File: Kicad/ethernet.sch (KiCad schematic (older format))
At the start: 26 parts, among them J12 RJ45_Amphenol_RJMG1BD3B8K1ANR, U11 DP83848C

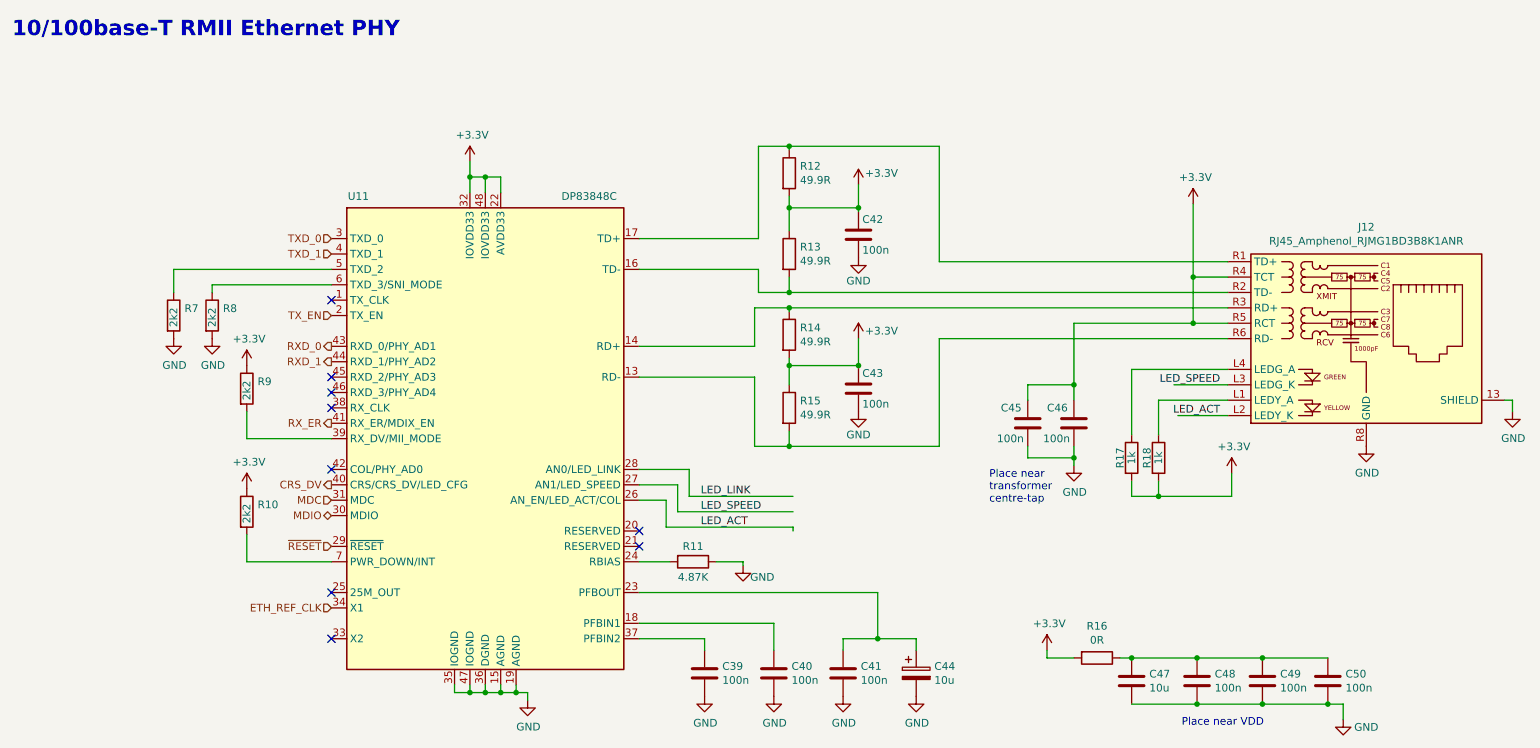
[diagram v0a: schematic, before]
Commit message: Removed USB FS hub. Added stacked USB A connector.
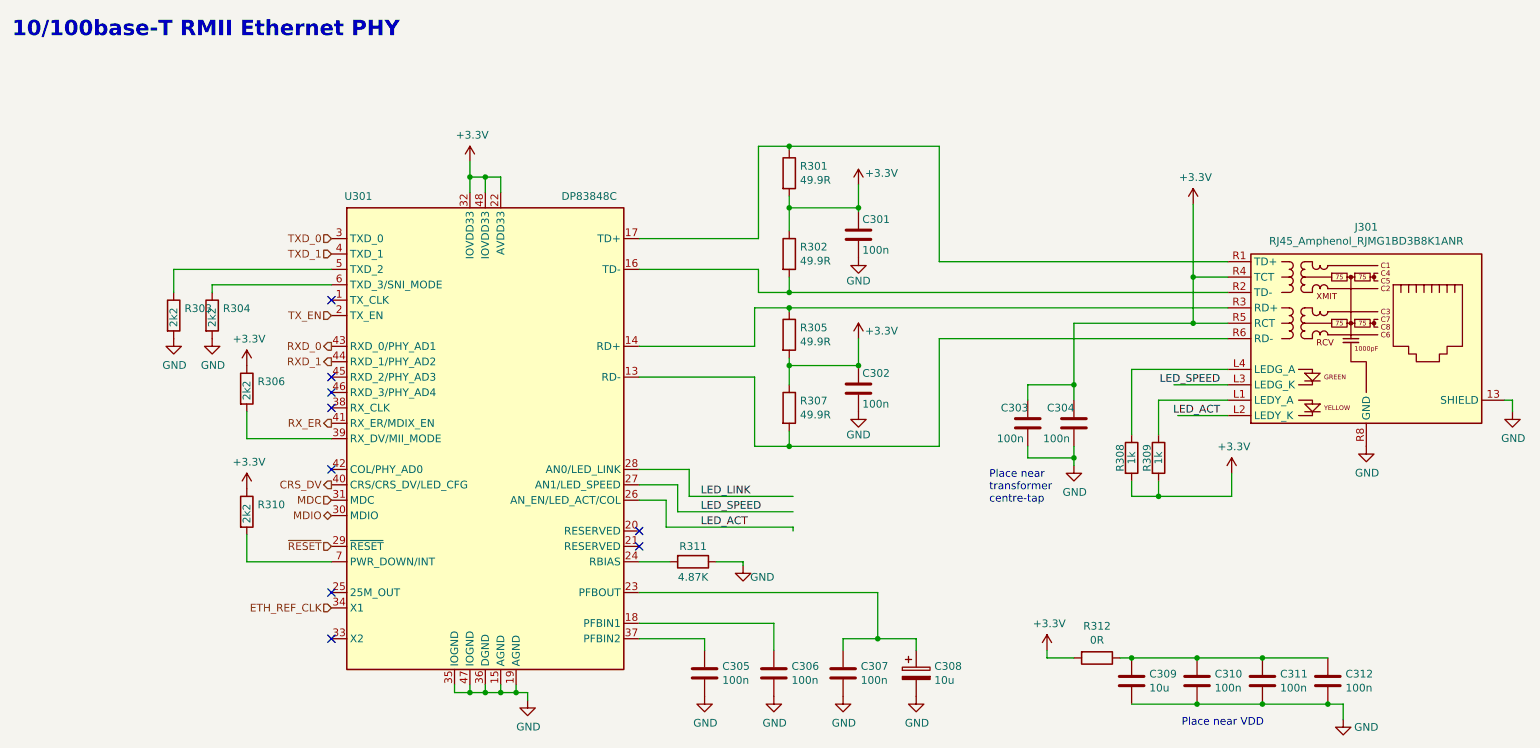
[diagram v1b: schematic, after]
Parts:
- C309: renamed from C47; footprint Capacitor_SMD:C_0402_1005Metric -> Capacitor_SMD:C_0805_2012Metric
- R301: renamed from R12; footprint (none) -> Resistor_SMD:R_0402_1005Metric
- R302: renamed from R13; footprint (none) -> Resistor_SMD:R_0402_1005Metric
- R303: renamed from R7; footprint (none) -> Resistor_SMD:R_0402_1005Metric
- R304: renamed from R8; footprint (none) -> Resistor_SMD:R_0402_1005Metric
- R305: renamed from R14; footprint (none) -> Resistor_SMD:R_0402_1005Metric
- R306: renamed from R9; footprint (none) -> Resistor_SMD:R_0402_1005Metric
- R307: renamed from R15; footprint (none) -> Resistor_SMD:R_0402_1005Metric
- R308: renamed from R17; footprint (none) -> Resistor_SMD:R_0402_1005Metric
- R309: renamed from R18; footprint (none) -> Resistor_SMD:R_0402_1005Metric
- R310: renamed from R10; footprint (none) -> Resistor_SMD:R_0402_1005Metric
- R311: renamed from R11; footprint (none) -> Resistor_SMD:R_0402_1005Metric
- R312: renamed from R16; footprint (none) -> Resistor_SMD:R_0402_1005Metric
- renumbered C42 to C301, C43 to C302, C45 to C303, C46 to C304, C39 to C305, C40 to C306, C41 to C307, C44 to C308, C48 to C310, C49 to C311, C50 to C312, J12 to J301, U11 to U301

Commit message: Schematic updates
Worked on USB Hub
Deleted QSPI SRAM
Added TSSOP-54 SDRAM (not wired up)
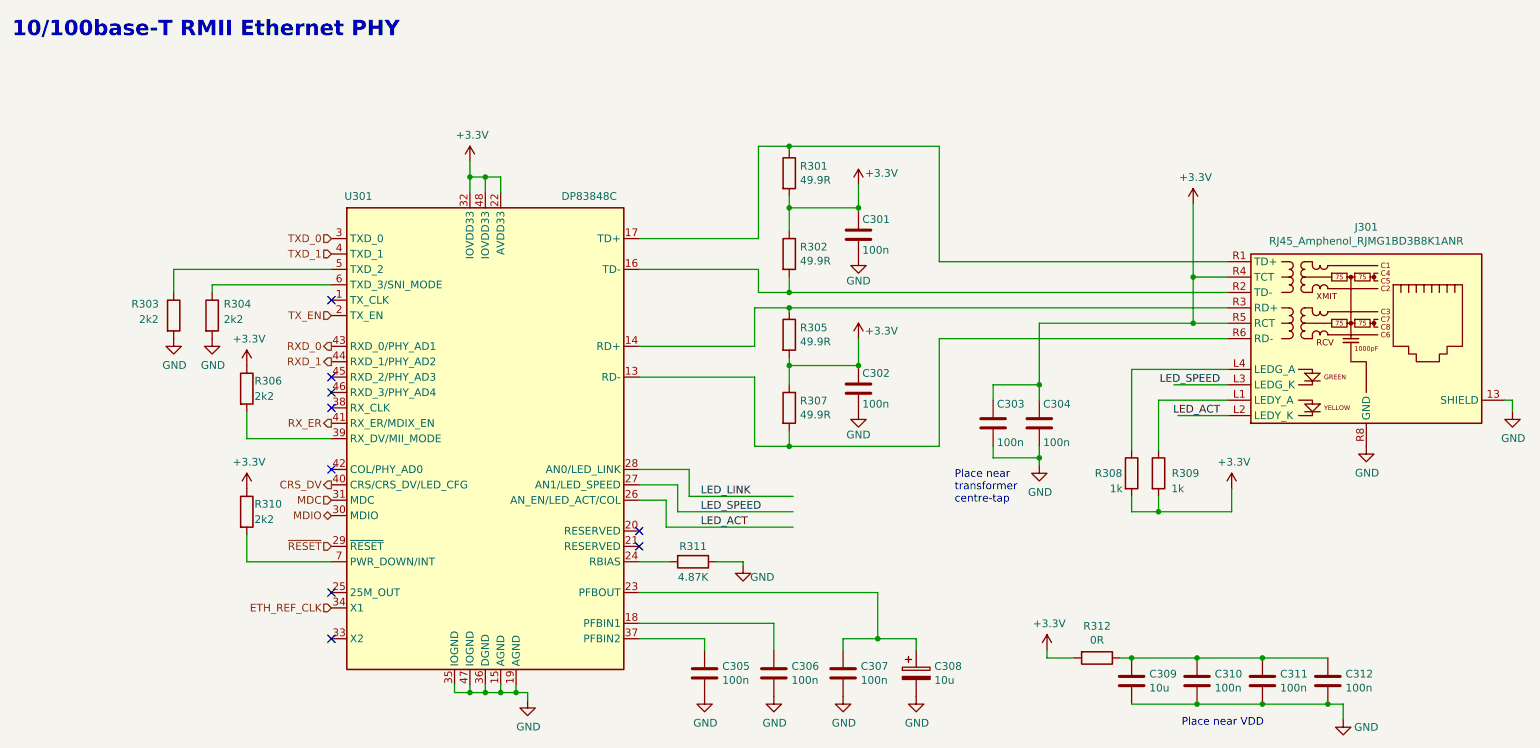
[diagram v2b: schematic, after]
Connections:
- wire segments 118 -> 117
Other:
- moved on the sheet: C303, C304, R308, R309
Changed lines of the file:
@@
 $Descr A4 11693 8268
 encoding utf-8
-Sheet 2 6
+Sheet 2 5
 Title "Neotron F7"
 Date "2020-05-25"
@@
 L Device:C C304
 U 1 1 5FA9EAF1
-P 7475 3275
-F 0 "C304" H 7300 3375 50  0000 L CNN
-F 1 "100n" H 7275 3175 50  0000 L CNN
-F 2 "Capacitor_SMD:C_0402_1005Metric" H 7513 3125 50  0001 C CNN
-F 3 "~" H 7475 3275 50  0001 C CNN
-F 4 "C1546" H 7475 3275 50  0001 C CNN "LCSC"
-	1    7475 3275
+P 7250 3275
+F 0 "C304" H 7275 3400 50  0000 L CNN
+F 1 "100n" H 7275 3150 50  0000 L CNN
+F 2 "Capacitor_SMD:C_0402_1005Metric" H 7288 3125 50  0001 C CNN
+F 3 "~" H 7250 3275 50  0001 C CNN
+F 4 "C1546" H 7250 3275 50  0001 C CNN "LCSC"
+	1    7250 3275
 	1    0    0    -1
 $EndComp
@@
 L Device:C C303
 U 1 1 5FA9EEAC
-P 7175 3275
-F 0 "C303" H 7000 3375 50  0000 L CNN
-F 1 "100n" H 6975 3175 50  0000 L CNN
-F 2 "Capacitor_SMD:C_0402_1005Metric" H 7213 3125 50  0001 C CNN
-F 3 "~" H 7175 3275 50  0001 C CNN
-F 4 "C1546" H 7175 3275 50  0001 C CNN "LCSC"
-	1    7175 3275
+P 6950 3275
+F 0 "C303" H 6975 3400 50  0000 L CNN
+F 1 "100n" H 6975 3150 50  0000 L CNN
+F 2 "Capacitor_SMD:C_0402_1005Metric" H 6988 3125 50  0001 C CNN
+F 3 "~" H 6950 3275 50  0001 C CNN
+F 4 "C1546" H 6950 3275 50  0001 C CNN "LCSC"
+	1    6950 3275
 	1    0    0    -1
 $EndComp
@@
 L power:GND #PWR0312
 U 1 1 5FA9F4E3
-P 7475 3550
-F 0 "#PWR0312" H 7475 3300 50  0001 C CNN
-F 1 "GND" H 7480 3377 50  0000 C CNN
-F 2 "" H 7475 3550 50  0001 C CNN
-F 3 "" H 7475 3550 50  0001 C CNN
-	1    7475 3550
+P 7250 3550
+F 0 "#PWR0312" H 7250 3300 50  0001 C CNN
+F 1 "GND" H 7255 3377 50  0000 C CNN
+F 2 "" H 7250 3550 50  0001 C CNN
+F 3 "" H 7250 3550 50  0001 C CNN
+	1    7250 3550
 	1    0    0    -1
 $EndComp
@@
 Connection ~ 5625 2900
 Connection ~ 6075 2900
-$Comp
-L power:+3.3V #PWR0313
-U 1 1 5FB0F0ED
-P 8500 3600
-F 0 "#PWR0313" H 8500 3450 50  0001 C CNN
-F 1 "+3.3V" H 8515 3773 50  0000 C CNN
-F 2 "" H 8500 3600 50  0001 C CNN
-F 3 "" H 8500 3600 50  0001 C CNN
-	1    8500 3600
-	1    0    0    -1
-$EndComp
-$Comp
-L Device:R R309
-U 1 1 5FB10B30
-P 8025 3500
-F 0 "R309" V 7950 3500 50  0000 C CNN
-F 1 "1k" V 8025 3500 50  0000 C CNN
-F 2 "Resistor_SMD:R_0402_1005Metric" V 7955 3500 50  0001 C CNN
-F 3 "~" H 8025 3500 50  0001 C CNN
-	1    8025 3500
-	1    0    0    -1
-$EndComp
-$Comp
-L Device:R R308
-U 1 1 5FB11481
-P 7850 3500
-F 0 "R308" V 7775 3500 50  0000 C CNN
-F 1 "1k" V 7850 3500 50  0000 C CNN
-F 2 "Resistor_SMD:R_0402_1005Metric" V 7780 3500 50  0001 C CNN
-F 3 "~" H 7850 3500 50  0001 C CNN
-	1    7850 3500
-	1    0    0    -1
-$EndComp
 Text Label 8425 3025 2    50   ~ 0
 LED_SPEED
@@
 Wire Wire Line
 	4825 3950 5650 3950
-Wire Wire Line
-	5650 3950 5650 3975
 Text Label 5050 3750 0    50   ~ 0
 LED_LINK
@@
 Text Label 5050 3950 0    50   ~ 0
 LED_ACT
-Text Notes 6925 3800 0    50   ~ 0
+Text Notes 6700 3800 0    50   ~ 0
 Place near\ntransformer\ncentre-tap
 NoConn ~ 4650 3975
@@
 	8475 3225 8150 3225
 Wire Wire Line
-	7850 2925 7850 3350
-Wire Wire Line
-	7850 3750 7850 3650
-Wire Wire Line
-	8025 3650 8025 3750
-Wire Wire Line
 	8475 3025 8125 3025
-Wire Wire Line
-	7850 3750 8025 3750
 $Comp
 L power:GND #PWR0311
@@
 	10325 3125 10325 3200
 Wire Wire Line
-	8500 3750 8500 3600
-Wire Wire Line
 	7850 2925 8475 2925
-Connection ~ 8025 3750
-Wire Wire Line
-	8025 3750 8500 3750
 Wire Wire Line
 	8475 3125 8025 3125
 Wire Wire Line
-	8025 3125 8025 3350
-Wire Wire Line
-	7475 3025 7175 3025
-Connection ~ 7475 3025
+	7250 3025 6950 3025
+Connection ~ 7250 3025
 Wire Wire Line
 	8250 2325 8475 2325
-Wire Wire Line
-	7475 2625 8250 2625
 Wire Wire Line
 	8250 2325 8250 2625
@@
 U 1 1 5EDDE40E
 P 1875 2575
-F 0 "R304" H 1945 2621 50  0000 L CNN
-F 1 "2k2" V 1875 2500 50  0000 L CNN
+F 0 "R304" H 1950 2650 50  0000 L CNN
+F 1 "2k2" H 1950 2550 50  0000 L CNN
 F 2 "Resistor_SMD:R_0402_1005Metric" V 1805 2575 50  0001 C CNN
 F 3 "~" H 1875 2575 50  0001 C CNN
@@
 U 1 1 5EDDE993
 P 1625 2575
-F 0 "R303" H 1695 2621 50  0000 L CNN
-F 1 "2k2" V 1625 2500 50  0000 L CNN
+F 0 "R303" H 1350 2650 50  0000 L CNN
+F 1 "2k2" H 1400 2550 50  0000 L CNN
 F 2 "Resistor_SMD:R_0402_1005Metric" V 1555 2575 50  0001 C CNN
 F 3 "~" H 1625 2575 50  0001 C CNN
@@
 U 1 1 5EDF11D2
 P 2100 3050
-F 0 "R306" H 2170 3096 50  0000 L CNN
-F 1 "2k2" V 2100 2975 50  0000 L CNN
+F 0 "R306" H 2150 3100 50  0000 L CNN
+F 1 "2k2" H 2150 3000 50  0000 L CNN
 F 2 "Resistor_SMD:R_0402_1005Metric" V 2030 3050 50  0001 C CNN
 F 3 "~" H 2100 3050 50  0001 C CNN
@@
 U 1 1 5EE02FB0
 P 2100 3850
-F 0 "R310" H 2170 3896 50  0000 L CNN
-F 1 "2k2" V 2100 3775 50  0000 L CNN
+F 0 "R310" H 2150 3900 50  0000 L CNN
+F 1 "2k2" H 2150 3800 50  0000 L CNN
 F 2 "Resistor_SMD:R_0402_1005Metric" V 2030 3850 50  0001 C CNN
 F 3 "~" H 2100 3850 50  0001 C CNN
@@
 Place near VDD
 Wire Wire Line
-	7175 3025 7175 3125
-Wire Wire Line
-	7475 3025 7475 3125
-Wire Wire Line
-	7475 2625 7475 3025
-Wire Wire Line
-	7175 3500 7475 3500
-Wire Wire Line
-	7175 3425 7175 3500
-Wire Wire Line
-	7475 3425 7475 3500
-Wire Wire Line
-	7475 3500 7475 3550
-Connection ~ 7475 3500
+	6950 3025 6950 3125
+Wire Wire Line
+	7250 3025 7250 3125
+Wire Wire Line
+	7250 2625 7250 3025
+Wire Wire Line
+	6950 3500 7250 3500
+Wire Wire Line
+	6950 3425 6950 3500
+Wire Wire Line
+	7250 3425 7250 3500
+Wire Wire Line
+	7250 3500 7250 3550
+Connection ~ 7250 3500
 Wire Wire Line
 	5400 2975 5400 3425
@@
 Text HLabel 2650 4475 0    50   Input ~ 0
 ETH_REF_CLK
+$Comp
+L power:+3.3V #PWR0313
+U 1 1 5FB0F0ED
+P 8500 3700
+F 0 "#PWR0313" H 8500 3550 50  0001 C CNN
+F 1 "+3.3V" H 8515 3873 50  0000 C CNN
+F 2 "" H 8500 3700 50  0001 C CNN
+F 3 "" H 8500 3700 50  0001 C CNN
+	1    8500 3700
+	1    0    0    -1
+$EndComp
+$Comp
+L Device:R R309
+U 1 1 5FB10B30
+P 8025 3600
+F 0 "R309" H 8200 3600 50  0000 C CNN
+F 1 "1k" H 8150 3500 50  0000 C CNN
+F 2 "Resistor_SMD:R_0402_1005Metric" V 7955 3600 50  0001 C CNN
+F 3 "~" H 8025 3600 50  0001 C CNN
+	1    8025 3600
+	1    0    0    -1
+$EndComp
+$Comp
+L Device:R R308
+U 1 1 5FB11481
+P 7850 3600
+F 0 "R308" H 7700 3600 50  0000 C CNN
+F 1 "1k" H 7750 3500 50  0000 C CNN
+F 2 "Resistor_SMD:R_0402_1005Metric" V 7780 3600 50  0001 C CNN
+F 3 "~" H 7850 3600 50  0001 C CNN
+	1    7850 3600
+	1    0    0    -1
+$EndComp
+Wire Wire Line
+	7850 3850 7850 3750
+Wire Wire Line
+	8025 3750 8025 3850
+Wire Wire Line
+	7850 3850 8025 3850
+Wire Wire Line
+	8500 3850 8500 3700
+Connection ~ 8025 3850
+Wire Wire Line
+	8025 3850 8500 3850
+Wire Wire Line
+	8025 3125 8025 3450
+Wire Wire Line
+	7850 2925 7850 3450
+Wire Wire Line
+	7250 2625 8250 2625
 $EndSCHEMATC

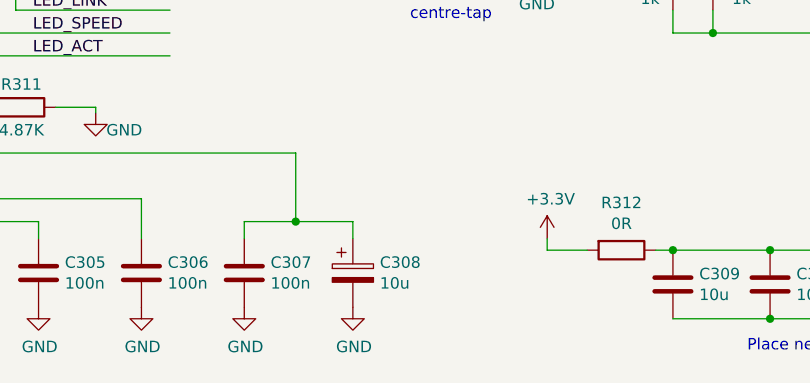
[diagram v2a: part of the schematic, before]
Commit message: Tidying up schematic, and README.
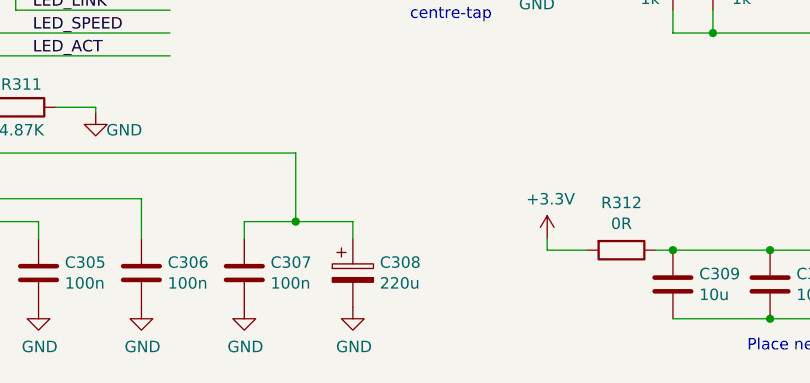
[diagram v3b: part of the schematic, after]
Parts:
- C308: value 10u -> 220u
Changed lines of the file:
@@
 $Descr A4 11693 8268
 encoding utf-8
-Sheet 2 5
+Sheet 2 9
 Title "Neotron F7"
 Date "2020-05-25"
@@
 P 6450 4900
 F 0 "C308" H 6568 4946 50  0000 L CNN
-F 1 "10u" H 6568 4855 50  0000 L CNN
+F 1 "220u" H 6568 4855 50  0000 L CNN
 F 2 "Capacitor_SMD:C_0805_2012Metric" H 6488 4750 50  0001 C CNN
 F 3 "~" H 6450 4900 50  0001 C CNN
